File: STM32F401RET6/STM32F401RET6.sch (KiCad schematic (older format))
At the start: 1 part

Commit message: append schematic
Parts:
- removed U?: STM32F401RETx, Package_QFP:LQFP-64_10x10mm_P0.5mm, symbol MCU_ST_STM32F4:STM32F401RETx
- added C?: 1uF, symbol Device:C
- added C?: 10uF, symbol Device:C
- added C? (x7): 0.1uF, symbol Device:C
- added C?: 4.7uF, symbol Device:C
- added R?: 10K, symbol Device:R
- added U?: STM32F401RETx, Package_QFP:LQFP-64_10x10mm_P0.5mm, symbol MCU_ST_STM32F4:STM32F401RETx
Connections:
- new net: C?.1, U?.30 (VCAP1)
- new net: R?.1, U?.60 (BOOT0)
- new net GND: C?.2, C?.2, C?.2, C?.2, C?.2, C?.2, C?.2, C?.2, C?.2, C?.2, R?.2, U?.12 (VSSA), U?.18 (VSS), U?.31 (VSS), U?.47 (VSS), U?.63 (VSS)
- new net PA0: U?.14 (PA0)
- new net PA1: U?.15 (PA1)
- new net PA10: U?.43 (PA10)
- new net PA11: U?.44 (PA11)
- new net PA12: U?.45 (PA12)
- new net PA15: U?.50 (PA15)
- new net PA2: U?.16 (PA2)
- new net PA3: U?.17 (PA3)
- new net PA4: U?.20 (PA4)
- new net PA5: U?.21 (PA5)
- new net PA6: U?.22 (PA6)
- new net PA7: U?.23 (PA7)
- new net PA8: U?.41 (PA8)
- new net PA9: U?.42 (PA9)
- new net PB0: U?.26 (PB0)
- new net PB1: U?.27 (PB1)
- new net PB10: U?.29 (PB10)
- new net PB12: U?.33 (PB12)
- new net PB13: U?.34 (PB13)
- new net PB14: U?.35 (PB14)
- new net PB15: U?.36 (PB15)
- new net PB2: U?.28 (PB2)
- new net PB4: U?.56 (PB4)
- new net PB5: U?.57 (PB5)
- new net PB6: U?.58 (PB6)
- new net PB7: U?.59 (PB7)
- new net PB8: U?.61 (PB8)
- new net PB9: U?.62 (PB9)
- new net PC0: U?.8 (PC0)
- new net PC1: U?.9 (PC1)
- new net PC10: U?.51 (PC10)
- new net PC11: U?.52 (PC11)
- new net PC12: U?.53 (PC12)
- new net PC13: U?.2 (PC13)
- new net PC14: U?.3 (PC14)
- new net PC15: U?.4 (PC15)
- new net PC2: U?.10 (PC2)
- new net PC3: U?.11 (PC3)
- new net PC4: U?.24 (PC4)
- new net PC5: U?.25 (PC5)
- new net PC6: U?.37 (PC6)
- new net PC7: U?.38 (PC7)
- new net PC8: U?.39 (PC8)
- new net PC9: U?.40 (PC9)
- new net PD2: U?.54 (PD2)
- new net PH0: U?.5 (PH0)
- new net PH1: U?.6 (PH1)
- new net SWCLK: U?.49 (PA14)
- new net SWDIO: U?.46 (PA13)
- new net SWO: U?.55 (PB3)
- new net VDD: C?.1, C?.1, C?.1, C?.1, C?.1, C?.1, C?.1, C?.1, U?.1 (VBAT), U?.13 (VREF+), U?.19 (VDD), U?.32 (VDD), U?.48 (VDD), U?.64 (VDD)
- new net nRST: C?.1, U?.7 (NRST)
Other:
- note added: "ADC1 IN14"
- note added: "ADC1 IN15"
- note added: "ADC1 IN8"
- note added: "ADC1 IN9"
- note added: "ADC1_IN10"
- note added: "ADC1_IN11"
- note added: "Boot from main flash memory"
- note added: "I2C1 SCL, SDIO D4"
- note added: "I2C1 SCL, USART1 TX"
- note added: "I2C1 SDA, USART1 RX"
- note added: "I2C3 SCL, USART1 CK, OTG FS SOF"
- note added: "I2C3 SMBA, USART1 TX, OTG FS VBUS"
- note added: "I2S CKIN, I2C3 SDA, SDIO D1"
- note added: "I2S2 MCK, UART6 TX, SDIO D6"
- note added: "I2S3 MCK, USART6 RX, SDIO D7"
- note added: "I2S3 ext_SD, SPI3 MISO, SDIO D3"
- note added: "No other pull-down cap needed"
- note added: "PH0/1 can be used as GPIO when external oscillator (HSE) is off"
- note added: "SDIO CMD"
- note added: "SPI1 MISO, ADC1 IN6"
- note added: "SPI1 MISO, SPI3 MISO, I2S3 ext_SD, I2C3 SDA"
- note added: "SPI1 MOSI, ADC1 IN7"
- note added: "SPI1 MOSI, SPI3 MOSI / I2S3 SD, I2C1 SMBA"
- note added: "SPI1 SCK, ADC1 IN5"
- note added: "SPI1 nSS, SPI3 nSS / I2S3 WS"
- note added: "SPI1 nSS, SPI3 nSS / I2S3 WS, USART2 CK, ADC1_IN4"
- note added: "SPI2 MISO, I2S2 ext_SD"
- note added: "SPI2 MISO, I2S2 ext_SD, ADC1_IN12"
- note added: "SPI2 MOSI / I2S2 SD"
- note added: "SPI2 MOSI, I2S2 SD, ADC1_IN13"
- note added: "SPI2 SCK / I2S2 CK"
- note added: "SPI2 SCK / I2S2 CK, I2C2 SCL"
- note added: "SPI2 nSS / I2S2 WS, I2C1 SDA, SDIO D5"
- note added: "SPI2 nSS / I2S2 WS, I2C2 SMBA"
- note added: "SPI3 MOSI / I2S3 SD, SDIO CK"
- note added: "SPI3 SCK / I2S3 CK, SDIO D2"
- note added: "USART1 CTS, USART6 TX, OTG FS DM"
- note added: "USART1 RTS, USART6 RX, OTG FS DP"
- note added: "USART1 RX, OTG FS ID"
- note added: "USART2 CTS, ADC1_IN0"
- note added: "USART2 RTS, ADC1_IN1"
- note added: "USART2 RX, ADC1_IN3"
- note added: "USART2 TX, ADC1_IN2"
- note added: "USART6 CK, SDIO D0"
- note added: "VBAT decoupling cap"
- note added: "VDD decoupling caps"
- note added: "VDDA decoupling caps\n"

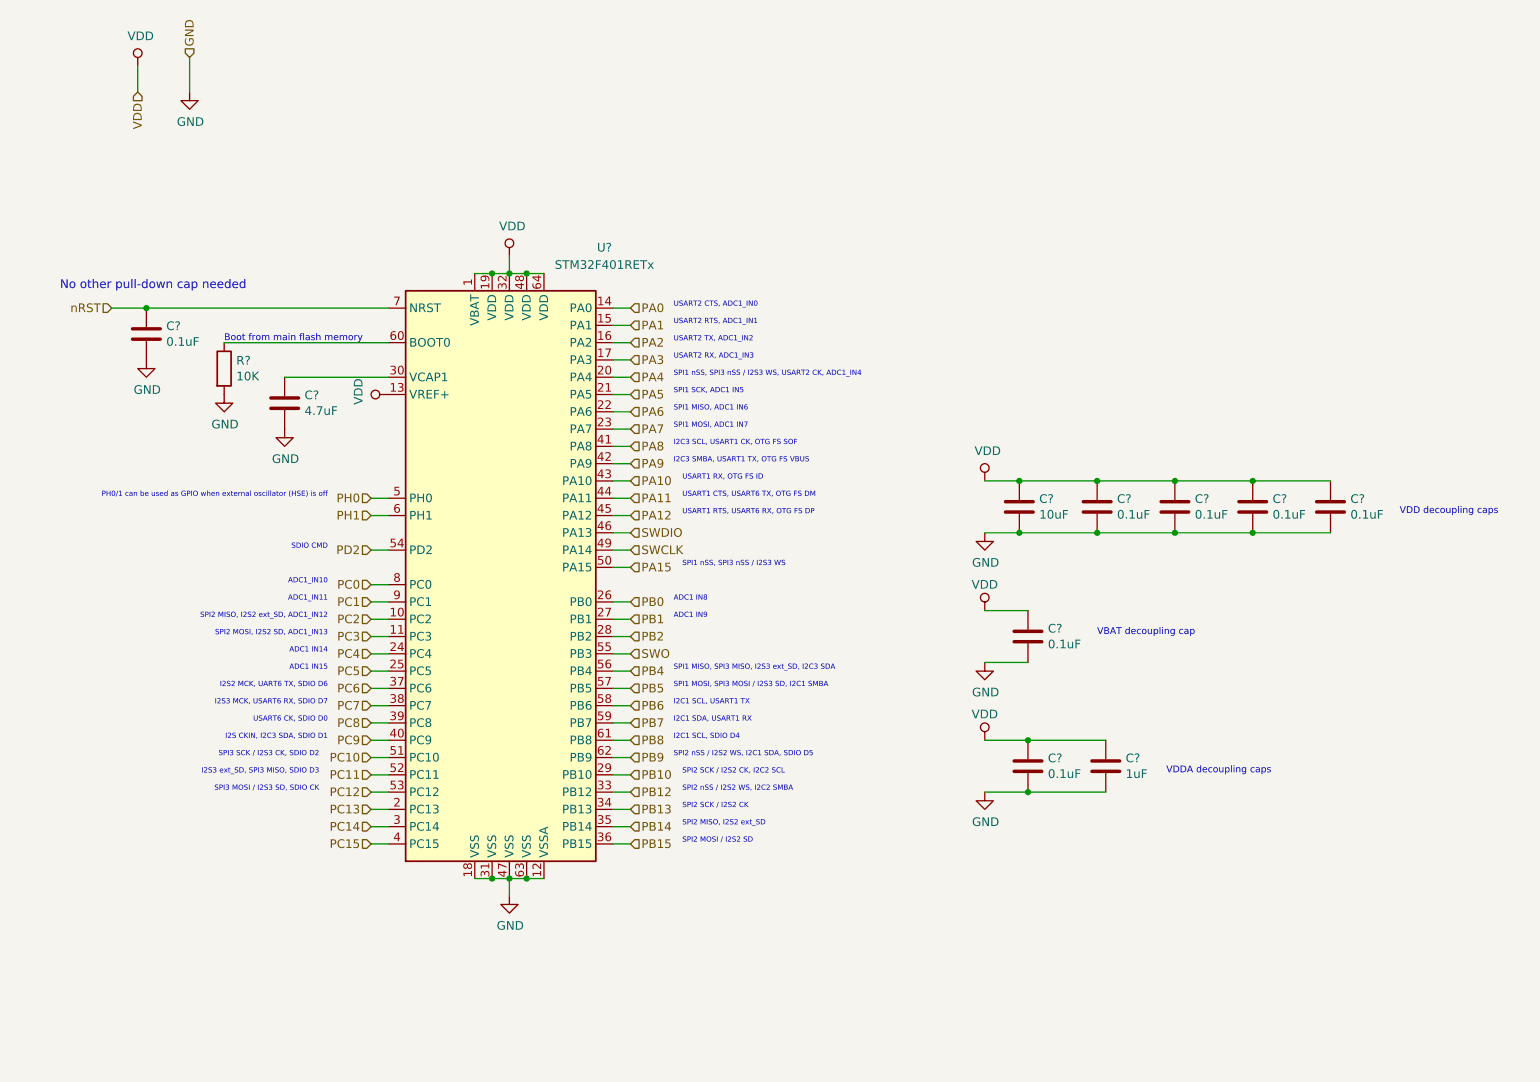
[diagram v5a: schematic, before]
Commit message: added RFM69HCW and titled the stm block
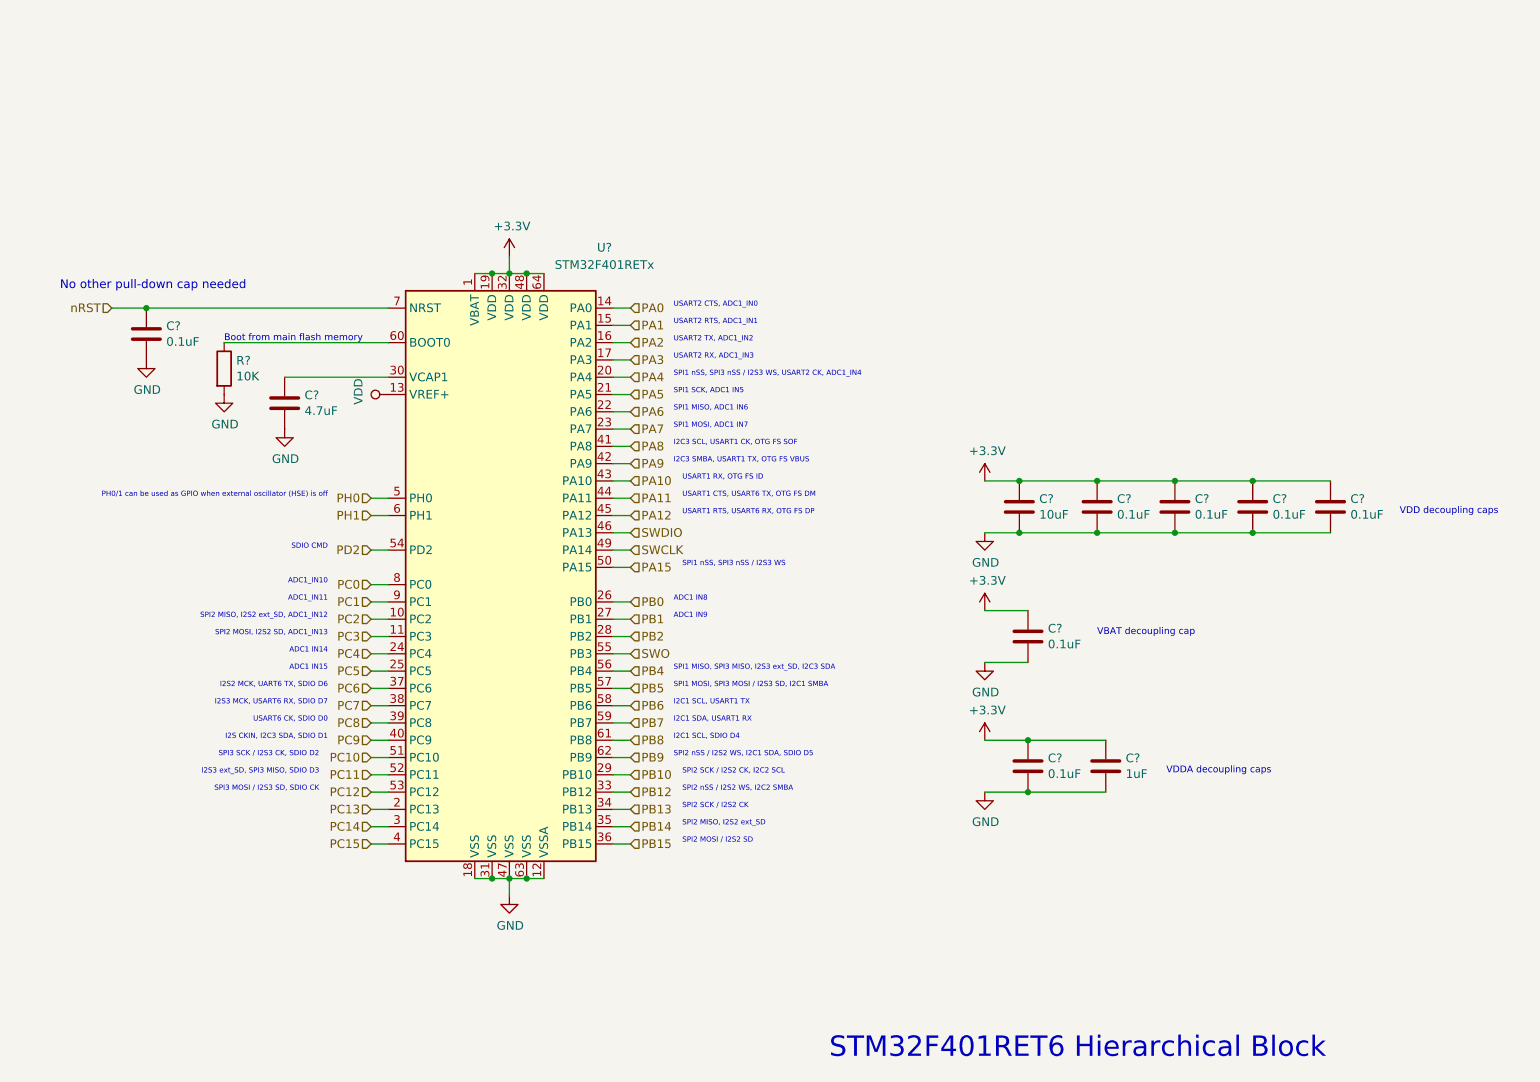
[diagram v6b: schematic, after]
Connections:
- net VDD: no longer C?.1, C?.1, C?.1, C?.1, C?.1, C?.1, C?.1, C?.1, U?.1 (VBAT), U?.19 (VDD), U?.32 (VDD), U?.48 (VDD), U?.64 (VDD)
- new net +3V3: C?.1, C?.1, C?.1, C?.1, C?.1, C?.1, C?.1, C?.1, U?.1 (VBAT), U?.19 (VDD), U?.32 (VDD), U?.48 (VDD), U?.64 (VDD)
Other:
- note added: "STM32F401RET6 Hierarchical Block"
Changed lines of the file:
@@
 	5150 5900 5050 5900
 Connection ~ 5150 5900
-$Comp
-L power:VDD #PWR?
-U 1 1 5DE18437
-P 5250 2300
-F 0 "#PWR?" H 5250 2150 50  0001 C CNN
-F 1 "VDD" H 5267 2473 50  0000 C CNN
-F 2 "" H 5250 2300 50  0001 C CNN
-F 3 "" H 5250 2300 50  0001 C CNN
-	1    5250 2300
-	1    0    0    -1
-$EndComp
 Wire Wire Line
 	5250 2300 5250 2400
 $Comp
-L power:GND #PWR?
+L power:GND #PWR0102
 U 1 1 5DE18883
 P 5250 6000
-F 0 "#PWR?" H 5250 5750 50  0001 C CNN
+F 0 "#PWR0102" H 5250 5750 50  0001 C CNN
 F 1 "GND" H 5255 5827 50  0000 C CNN
 F 2 "" H 5250 6000 50  0001 C CNN
@@
 $EndComp
 $Comp
-L power:VDD #PWR?
-U 1 1 5DE18DA9
-P 8000 3600
-F 0 "#PWR?" H 8000 3450 50  0001 C CNN
-F 1 "VDD" H 8017 3773 50  0000 C CNN
-F 2 "" H 8000 3600 50  0001 C CNN
-F 3 "" H 8000 3600 50  0001 C CNN
-	1    8000 3600
-	1    0    0    -1
-$EndComp
-$Comp
-L power:GND #PWR?
+L power:GND #PWR0104
 U 1 1 5DE18B06
 P 8000 3900
-F 0 "#PWR?" H 8000 3650 50  0001 C CNN
+F 0 "#PWR0104" H 8000 3650 50  0001 C CNN
 F 1 "GND" H 8005 3727 50  0000 C CNN
 F 2 "" H 8000 3900 50  0001 C CNN
@@
 $EndComp
 $Comp
-L power:VDD #PWR?
-U 1 1 5DE1D5D0
-P 8000 4350
-F 0 "#PWR?" H 8000 4200 50  0001 C CNN
-F 1 "VDD" H 8000 4500 50  0000 C CNN
-F 2 "" H 8000 4350 50  0001 C CNN
-F 3 "" H 8000 4350 50  0001 C CNN
-	1    8000 4350
-	1    0    0    -1
-$EndComp
-$Comp
-L power:GND #PWR?
+L power:GND #PWR0106
 U 1 1 5DE1D921
 P 8000 4650
-F 0 "#PWR?" H 8000 4400 50  0001 C CNN
+F 0 "#PWR0106" H 8000 4400 50  0001 C CNN
 F 1 "GND" H 8005 4477 50  0000 C CNN
 F 2 "" H 8000 4650 50  0001 C CNN
@@
 $EndComp
 $Comp
-L power:VDD #PWR?
-U 1 1 5DE1EE4C
-P 8000 5100
-F 0 "#PWR?" H 8000 4950 50  0001 C CNN
-F 1 "VDD" H 8000 5250 50  0000 C CNN
-F 2 "" H 8000 5100 50  0001 C CNN
-F 3 "" H 8000 5100 50  0001 C CNN
-	1    8000 5100
-	1    0    0    -1
-$EndComp
-$Comp
-L power:GND #PWR?
+L power:GND #PWR0108
 U 1 1 5DE1F4FA
 P 8000 5400
-F 0 "#PWR?" H 8000 5150 50  0001 C CNN
+F 0 "#PWR0108" H 8000 5150 50  0001 C CNN
 F 1 "GND" H 8005 5227 50  0000 C CNN
 F 2 "" H 8000 5400 50  0001 C CNN
@@
 VDD decoupling caps
 $Comp
-L power:VDD #PWR?
+L power:VDD #PWR0109
 U 1 1 5DE19EB9
 P 4550 3100
-F 0 "#PWR?" H 4550 2950 50  0001 C CNN
+F 0 "#PWR0109" H 4550 2950 50  0001 C CNN
 F 1 "VDD" H 4567 3273 50  0000 C CNN
 F 2 "" H 4550 3100 50  0001 C CNN
@@
 $EndComp
 $Comp
-L power:GND #PWR?
+L power:GND #PWR0110
 U 1 1 5DE1B283
 P 3950 3300
-F 0 "#PWR?" H 3950 3050 50  0001 C CNN
+F 0 "#PWR0110" H 3950 3050 50  0001 C CNN
 F 1 "GND" H 3955 3127 50  0000 C CNN
 F 2 "" H 3950 3300 50  0001 C CNN
@@
 	2950 2600 3150 2600
 $Comp
-L power:GND #PWR?
+L power:GND #PWR0111
 U 1 1 5DE1D367
 P 3150 2900
-F 0 "#PWR?" H 3150 2650 50  0001 C CNN
+F 0 "#PWR0111" H 3150 2650 50  0001 C CNN
 F 1 "GND" H 3155 2727 50  0000 C CNN
 F 2 "" H 3150 2900 50  0001 C CNN
@@
 $EndComp
 $Comp
-L power:GND #PWR?
+L power:GND #PWR0112
 U 1 1 5DE1E857
 P 3600 3100
-F 0 "#PWR?" H 3600 2850 50  0001 C CNN
+F 0 "#PWR0112" H 3600 2850 50  0001 C CNN
 F 1 "GND" H 3605 2927 50  0000 C CNN
 F 2 "" H 3600 3100 50  0001 C CNN
@@
 Wire Wire Line
 	5950 3900 5850 3900
-$Comp
-L power:VDD #PWR?
-U 1 1 5DE18ECC
-P 3100 1200
-F 0 "#PWR?" H 3100 1050 50  0001 C CNN
-F 1 "VDD" H 3117 1373 50  0000 C CNN
-F 2 "" H 3100 1200 50  0001 C CNN
-F 3 "" H 3100 1200 50  0001 C CNN
-	1    3100 1200
-	1    0    0    -1
-$EndComp
-$Comp
-L power:GND #PWR?
-U 1 1 5DE19178
-P 3400 1350
-F 0 "#PWR?" H 3400 1100 50  0001 C CNN
-F 1 "GND" H 3405 1177 50  0000 C CNN
-F 2 "" H 3400 1350 50  0001 C CNN
-F 3 "" H 3400 1350 50  0001 C CNN
-	1    3400 1350
-	1    0    0    -1
-$EndComp
-Text HLabel 3100 1350 3    50   Input ~ 0
-VDD
-Wire Wire Line
-	3100 1350 3100 1200
-Text HLabel 3400 1150 1    50   Input ~ 0
-GND
-Wire Wire Line
-	3400 1150 3400 1350
 Text HLabel 5950 2600 2    50   Input ~ 0
 PA0
@@
 Text Notes 6200 5200 0    30   ~ 0
 SPI2 nSS / I2S2 WS, I2C1 SDA, SDIO D5
+$Comp
+L power:+3.3V #PWR?
+U 1 1 5DE1F0DC
+P 5250 2300
+F 0 "#PWR?" H 5250 2150 50  0001 C CNN
+F 1 "+3.3V" H 5265 2473 50  0000 C CNN
+F 2 "" H 5250 2300 50  0001 C CNN
+F 3 "" H 5250 2300 50  0001 C CNN
+	1    5250 2300
+	1    0    0    -1
+$EndComp
+$Comp
+L power:+3.3V #PWR?
+U 1 1 5DE22E45
+P 8000 3600
+F 0 "#PWR?" H 8000 3450 50  0001 C CNN
+F 1 "+3.3V" H 8015 3773 50  0000 C CNN
+F 2 "" H 8000 3600 50  0001 C CNN
+F 3 "" H 8000 3600 50  0001 C CNN
+	1    8000 3600
+	1    0    0    -1
+$EndComp
+$Comp
+L power:+3.3V #PWR?
+U 1 1 5DE235AC
+P 8000 4350
+F 0 "#PWR?" H 8000 4200 50  0001 C CNN
+F 1 "+3.3V" H 8015 4523 50  0000 C CNN
+F 2 "" H 8000 4350 50  0001 C CNN
+F 3 "" H 8000 4350 50  0001 C CNN
+	1    8000 4350
+	1    0    0    -1
+$EndComp
+$Comp
+L power:+3.3V #PWR?
+U 1 1 5DE2397A
+P 8000 5100
+F 0 "#PWR?" H 8000 4950 50  0001 C CNN
+F 1 "+3.3V" H 8015 5273 50  0000 C CNN
+F 2 "" H 8000 5100 50  0001 C CNN
+F 3 "" H 8000 5100 50  0001 C CNN
+	1    8000 5100
+	1    0    0    -1
+$EndComp
+Text Notes 7100 6950 0    118  ~ 0
+STM32F401RET6 Hierarchical Block
 $EndSCHEMATC

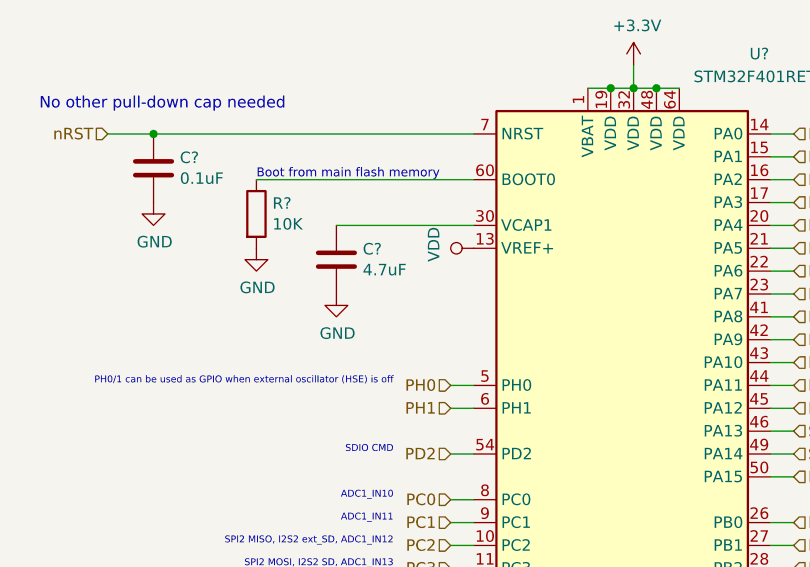
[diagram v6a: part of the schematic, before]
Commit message: updates to rfm and fix on pwr for stm
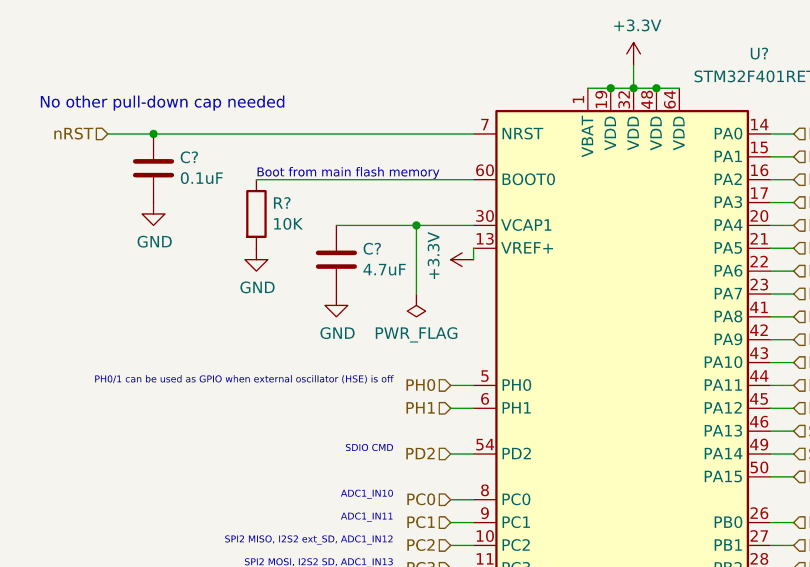
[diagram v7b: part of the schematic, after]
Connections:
- net VDD is gone; now on net +3V3: U?.13 (VREF+)
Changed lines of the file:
@@
 VDD decoupling caps
-$Comp
-L power:VDD #PWR0109
-U 1 1 5DE19EB9
-P 4550 3100
-F 0 "#PWR0109" H 4550 2950 50  0001 C CNN
-F 1 "VDD" H 4567 3273 50  0000 C CNN
-F 2 "" H 4550 3100 50  0001 C CNN
-F 3 "" H 4550 3100 50  0001 C CNN
-	1    4550 3100
-	0    -1   -1   0
-$EndComp
 $Comp
 L Device:C C?
@@
 $EndComp
 Wire Wire Line
-	3950 3000 4550 3000
+	3950 3000 4300 3000
 $Comp
 L Device:C C?
@@
 Text Notes 7100 6950 0    118  ~ 0
 STM32F401RET6 Hierarchical Block
+$Comp
+L power:+3.3V #PWR?
+U 1 1 5DE2F79B
+P 4550 3150
+F 0 "#PWR?" H 4550 3000 50  0001 C CNN
+F 1 "+3.3V" H 4565 3323 50  0000 C CNN
+F 2 "" H 4550 3150 50  0001 C CNN
+F 3 "" H 4550 3150 50  0001 C CNN
+	1    4550 3150
+	0    -1   -1   0
+$EndComp
+Wire Wire Line
+	4550 3100 4550 3150
+$Comp
+L power:PWR_FLAG #FLG?
+U 1 1 5DE3436C
+P 4300 3300
+F 0 "#FLG?" H 4300 3375 50  0001 C CNN
+F 1 "PWR_FLAG" H 4300 3473 50  0000 C CNN
+F 2 "" H 4300 3300 50  0001 C CNN
+F 3 "~" H 4300 3300 50  0001 C CNN
+	1    4300 3300
+	-1   0    0    1
+$EndComp
+Wire Wire Line
+	4300 3300 4300 3000
+Connection ~ 4300 3000
+Wire Wire Line
+	4300 3000 4550 3000
 $EndSCHEMATC
